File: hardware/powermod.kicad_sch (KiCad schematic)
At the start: 72 parts, among them J1 USB_C_IN, J2 USB_C_OUT, J3 JST_PH_2, J4 STEMMA_QT, J5 UPDI_HDR, Q1 AON7407, Q2 AON7407, Q3 BSS138, SW1 BUTTON, U1 BM8563, U2 ATtiny1617, U3 TPS63020DSJR, U4 TP4056, U5 XC6206P332MR, Y1 32.768kHz

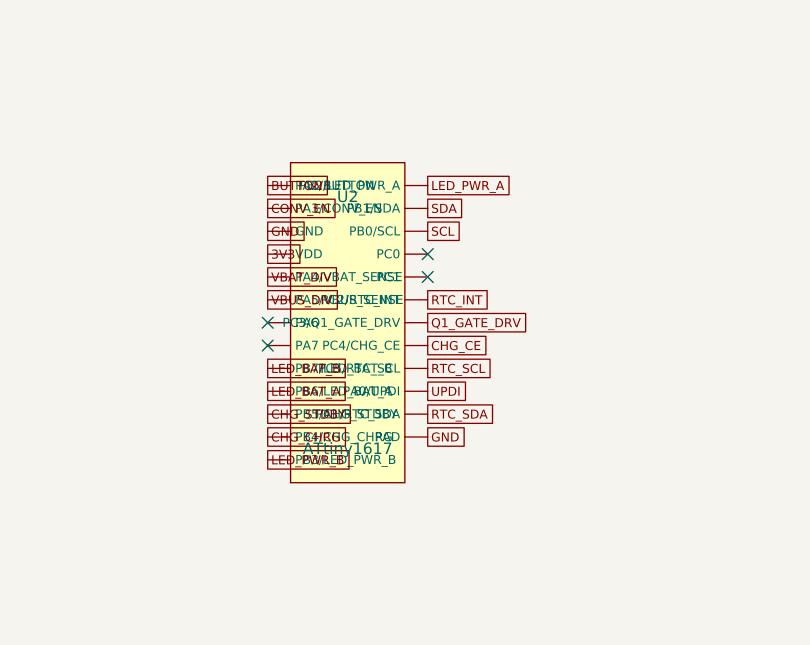
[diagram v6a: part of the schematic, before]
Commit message: attiny: swap MCU to ATtiny1616 SOIC-20 — breaks the QFN routing wall
The 24-pin QFN (0.5mm pitch) was the persistent autorouting blocker: two of
its pins could never escape, boxed in by their routed neighbours, and no
placement or router technique moved them. Swapping to the ATtiny1616 in
SOIC-20 (1.27mm pitch, 2.5x coarser, no exposed pad, hand-solderable) removes
that wall entirely -- verified: the MCU pins (3V3, Q1_GATE_DRV) that were stuck
across every prior attempt now route, and the residual is ordinary nets
(VBUS/VOUT pour connections, GND stitching), no escape wall.

Electrical: we used exactly 18 signals and the SOIC-20 has exactly 18 I/O, so
it fits -- at the cost of the 4 spare pins the 24-pin had. Four signals moved
off pins the 20-pin package lacks (LED_BAT_A/B off PB6/PB7 -> PA6/PA7, CHG_CE
off PC4 -> PC0, RTC_SCL off PC5 -> PC1); all are plain GPIO and the async-wake
(PC2/PA2), TWI (PB0/PB1), ADC (PA4/PA5) and UPDI (PA0) pins are unchanged.

Pinout taken from KiCad's ATtiny406-S base symbol (the shared 20-pin tinyAVR-1
map), NOT a web summary (which had it wrong). Footprint SOIC-20W_7.5x12.8mm.
LCSC C2891852 to confirm at order time. netlist self-test + ERC both clean
(72 components, 231 pins). On the attiny-soic20 branch.

Co-Authored-By: Claude Opus 4.8 <noreply@anthropic.com>
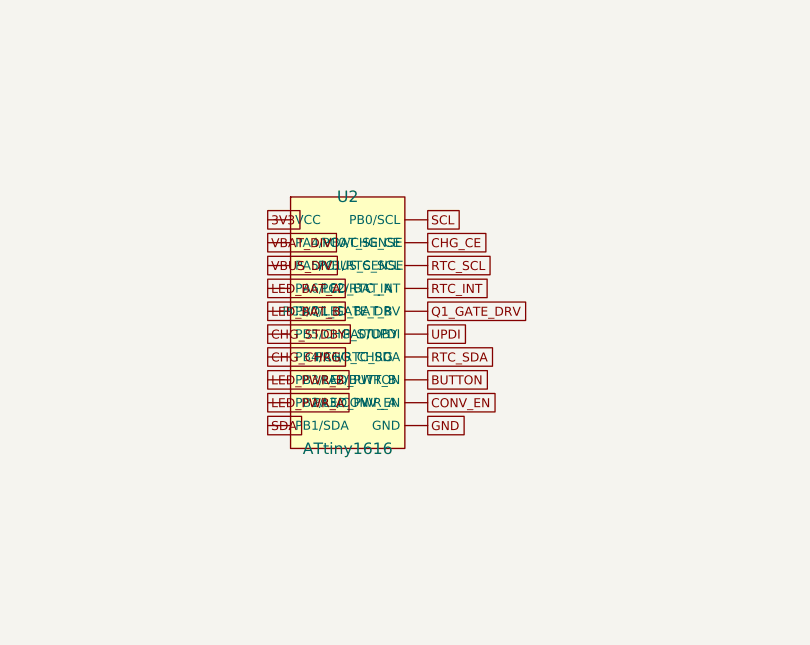
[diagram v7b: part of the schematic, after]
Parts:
- U2: value ATtiny1617 -> ATtiny1616; footprint Package_DFN_QFN:QFN-24-1EP_4x4mm_P0.5mm_EP2.6x2.6mm -> Package_SO:SOIC-20W_7.5x12.8mm_P1.27mm
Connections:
- net 3V3: now also U2.1 (VCC); no longer U2.4 (VDD)
- net BUTTON: now also U2.18 (PA2/BUTTON); no longer U2.1 (PA2/BUTTON)
- net CHG_CE: now also U2.12 (PC0/CHG_CE); no longer U2.21 (PC4/CHG_CE)
- net CHG_CHRG: now also U2.7 (PB4/CHG_CHRG); no longer U2.12 (PB4/CHG_CHRG)
- net CHG_STDBY: now also U2.6 (PB5/CHG_STDBY); no longer U2.11 (PB5/CHG_STDBY)
- net CONV_EN: now also U2.19 (PA3/CONV_EN); no longer U2.2 (PA3/CONV_EN)
- net GND: now also U2.20 (GND); no longer U2.25 (PAD), U2.3 (GND)
- net LED_BAT_A: now also U2.4 (PA6/LED_BAT_A); no longer U2.10 (PB6/LED_BAT_A)
- net LED_BAT_B: now also U2.5 (PA7/LED_BAT_B); no longer U2.9 (PB7/LED_BAT_B)
- net LED_PWR_A: now also U2.9 (PB2/LED_PWR_A); no longer U2.14 (PB2/LED_PWR_A)
- net LED_PWR_B: now also U2.8 (PB3/LED_PWR_B); no longer U2.13 (PB3/LED_PWR_B)
- net Q1_GATE_DRV: now also U2.15 (PC3/Q1_GATE_DRV); no longer U2.20 (PC3/Q1_GATE_DRV)
- net RTC_INT: now also U2.14 (PC2/RTC_INT); no longer U2.19 (PC2/RTC_INT)
- net RTC_SCL: now also U2.13 (PC1/RTC_SCL); no longer U2.22 (PC5/RTC_SCL)
- net RTC_SDA: now also U2.17 (PA1/RTC_SDA); no longer U2.24 (PA1/RTC_SDA)
- net SCL: now also U2.11 (PB0/SCL); no longer U2.16 (PB0/SCL)
- net SDA: now also U2.10 (PB1/SDA); no longer U2.15 (PB1/SDA)
- net UPDI: now also U2.16 (PA0/UPDI); no longer U2.23 (PA0/UPDI)
- net VBAT_DIV: now also U2.2 (PA4/VBAT_SENSE); no longer U2.5 (PA4/VBAT_SENSE)
- net VBUS_DIV: now also U2.3 (PA5/VBUS_SENSE); no longer U2.6 (PA5/VBUS_SENSE)
- no-connect marks 15 -> 11
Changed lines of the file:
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@@
  (symbol (lib_id "powermod:PM_U2") (at 670.5600000000001 294.64000000000004 0) (unit 1) (in_bom yes) (on_board yes)
   (property "Reference" "U2" (at 670.5600000000001 280.64000000000004 0) (effects (font (size 1.27 1.27))))
-  (property "Value" "ATtiny1617" (at 670.5600000000001 308.64000000000004 0) (effects (font (size 1.27 1.27))))
-  (property "Footprint" "Package_DFN_QFN:QFN-24-1EP_4x4mm_P0.5mm_EP2.6x2.6mm" (at 670.5600000000001 294.64000000000004 0) (effects (font (size 1.27 1.27)) hide))
+  (property "Value" "ATtiny1616" (at 670.5600000000001 308.64000000000004 0) (effects (font (size 1.27 1.27))))
+  (property "Footprint" "Package_SO:SOIC-20W_7.5x12.8mm_P1.27mm" (at 670.5600000000001 294.64000000000004 0) (effects (font (size 1.27 1.27)) hide))
   (pin "1")
   (pin "2")
@@
   (pin "18")
   (pin "19")
-  (pin "20")
-  (pin "21")
-  (pin "22")
-  (pin "23")
-  (pin "24")
-  (pin "25"))
+  (pin "20"))
  (symbol (lib_id "powermod:PM_U3") (at 670.5600000000001 360.68000000000006 0) (unit 1) (in_bom yes) (on_board yes)
   (property "Reference" "U3" (at 670.5600000000001 346.68000000000006 0) (effects (font (size 1.27 1.27))))
@@
  (global_label "RTC_SCL" (shape passive) (at 679.45 227.32999999999998 0) (effects (font (size 1.0 1.0)) (justify left)))
  (global_label "RTC_VDD" (shape passive) (at 679.45 232.41 0) (effects (font (size 1.0 1.0)) (justify left)))
- (global_label "BUTTON" (shape passive) (at 661.6700000000001 279.40000000000003 0) (effects (font (size 1.0 1.0)) (justify left)))
- (global_label "CONV_EN" (shape passive) (at 661.6700000000001 281.94000000000005 0) (effects (font (size 1.0 1.0)) (justify left)))
- (global_label "GND" (shape passive) (at 661.6700000000001 284.48 0) (effects (font (size 1.0 1.0)) (justify left)))
- (global_label "3V3" (shape passive) (at 661.6700000000001 287.02000000000004 0) (effects (font (size 1.0 1.0)) (justify left)))
- (global_label "VBAT_DIV" (shape passive) (at 661.6700000000001 289.56000000000006 0) (effects (font (size 1.0 1.0)) (justify left)))
- (global_label "VBUS_DIV" (shape passive) (at 661.6700000000001 292.1 0) (effects (font (size 1.0 1.0)) (justify left)))
- (global_label "LED_BAT_B" (shape passive) (at 661.6700000000001 299.72 0) (effects (font (size 1.0 1.0)) (justify left)))
- (global_label "LED_BAT_A" (shape passive) (at 661.6700000000001 302.26000000000005 0) (effects (font (size 1.0 1.0)) (justify left)))
- (global_label "CHG_STDBY" (shape passive) (at 661.6700000000001 304.80000000000007 0) (effects (font (size 1.0 1.0)) (justify left)))
- (global_label "CHG_CHRG" (shape passive) (at 661.6700000000001 307.34000000000003 0) (effects (font (size 1.0 1.0)) (justify left)))
- (global_label "LED_PWR_B" (shape passive) (at 661.6700000000001 309.88000000000005 0) (effects (font (size 1.0 1.0)) (justify left)))
- (global_label "LED_PWR_A" (shape passive) (at 679.45 279.40000000000003 0) (effects (font (size 1.0 1.0)) (justify left)))
- (global_label "SDA" (shape passive) (at 679.45 281.94000000000005 0) (effects (font (size 1.0 1.0)) (justify left)))
- (global_label "SCL" (shape passive) (at 679.45 284.48 0) (effects (font (size 1.0 1.0)) (justify left)))
- (global_label "RTC_INT" (shape passive) (at 679.45 292.1 0) (effects (font (size 1.0 1.0)) (justify left)))
- (global_label "Q1_GATE_DRV" (shape passive) (at 679.45 294.64000000000004 0) (effects (font (size 1.0 1.0)) (justify left)))
- (global_label "CHG_CE" (shape passive) (at 679.45 297.18000000000006 0) (effects (font (size 1.0 1.0)) (justify left)))
- (global_label "RTC_SCL" (shape passive) (at 679.45 299.72 0) (effects (font (size 1.0 1.0)) (justify left)))
- (global_label "UPDI" (shape passive) (at 679.45 302.26000000000005 0) (effects (font (size 1.0 1.0)) (justify left)))
- (global_label "RTC_SDA" (shape passive) (at 679.45 304.80000000000007 0) (effects (font (size 1.0 1.0)) (justify left)))
- (global_label "GND" (shape passive) (at 679.45 307.34000000000003 0) (effects (font (size 1.0 1.0)) (justify left)))
+ (global_label "3V3" (shape passive) (at 661.6700000000001 283.21000000000004 0) (effects (font (size 1.0 1.0)) (justify left)))
+ (global_label "VBAT_DIV" (shape passive) (at 661.6700000000001 285.75000000000006 0) (effects (font (size 1.0 1.0)) (justify left)))
+ (global_label "VBUS_DIV" (shape passive) (at 661.6700000000001 288.29 0) (effects (font (size 1.0 1.0)) (justify left)))
+ (global_label "LED_BAT_A" (shape passive) (at 661.6700000000001 290.83000000000004 0) (effects (font (size 1.0 1.0)) (justify left)))
+ (global_label "LED_BAT_B" (shape passive) (at 661.6700000000001 293.37000000000006 0) (effects (font (size 1.0 1.0)) (justify left)))
+ (global_label "CHG_STDBY" (shape passive) (at 661.6700000000001 295.91 0) (effects (font (size 1.0 1.0)) (justify left)))
+ (global_label "CHG_CHRG" (shape passive) (at 661.6700000000001 298.45000000000005 0) (effects (font (size 1.0 1.0)) (justify left)))
+ (global_label "LED_PWR_B" (shape passive) (at 661.6700000000001 300.99000000000007 0) (effects (font (size 1.0 1.0)) (justify left)))
+ (global_label "LED_PWR_A" (shape passive) (at 661.6700000000001 303.53000000000003 0) (effects (font (size 1.0 1.0)) (justify left)))
+ (global_label "SDA" (shape passive) (at 661.6700000000001 306.07000000000005 0) (effects (font (size 1.0 1.0)) (justify left)))
+ (global_label "SCL" (shape passive) (at 679.45 283.21000000000004 0) (effects (font (size 1.0 1.0)) (justify left)))
+ (global_label "CHG_CE" (shape passive) (at 679.45 285.75000000000006 0) (effects (font (size 1.0 1.0)) (justify left)))
+ (global_label "RTC_SCL" (shape passive) (at 679.45 288.29 0) (effects (font (size 1.0 1.0)) (justify left)))
+ (global_label "RTC_INT" (shape passive) (at 679.45 290.83000000000004 0) (effects (font (size 1.0 1.0)) (justify left)))
+ (global_label "Q1_GATE_DRV" (shape passive) (at 679.45 293.37000000000006 0) (effects (font (size 1.0 1.0)) (justify left)))
+ (global_label "UPDI" (shape passive) (at 679.45 295.91 0) (effects (font (size 1.0 1.0)) (justify left)))
+ (global_label "RTC_SDA" (shape passive) (at 679.45 298.45000000000005 0) (effects (font (size 1.0 1.0)) (justify left)))
+ (global_label "BUTTON" (shape passive) (at 679.45 300.99000000000007 0) (effects (font (size 1.0 1.0)) (justify left)))
+ (global_label "CONV_EN" (shape passive) (at 679.45 303.53000000000003 0) (effects (font (size 1.0 1.0)) (justify left)))
+ (global_label "GND" (shape passive) (at 679.45 306.07000000000005 0) (effects (font (size 1.0 1.0)) (justify left)))
  (global_label "VSYS" (shape passive) (at 661.6700000000001 351.7900000000001 0) (effects (font (size 1.0 1.0)) (justify left)))
  (global_label "GND" (shape passive) (at 661.6700000000001 354.33000000000004 0) (effects (font (size 1.0 1.0)) (justify left)))
@@
  (no_connect (at 234.95 163.83))
  (no_connect (at 679.45 229.87))
- (no_connect (at 661.6700000000001 294.64000000000004))
- (no_connect (at 661.6700000000001 297.18000000000006))
- (no_connect (at 679.45 287.02000000000004))
- (no_connect (at 679.45 289.56000000000006))
  (no_connect (at 679.45 364.49000000000007))
 )

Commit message: hardware: pre-fab audit + D5 supercap-drain fix; mount board final
Full pre-fab audit (PREFAB_AUDIT.md): board verified pad-for-pad against
netlist.py (214/214 + 11 NC), every IC pinout re-checked against datasheets,
all operating points computed (FB divider exactly 5.000/3.278V via JP2, ADC
ranges, gate drive, ~7.5uA off-state drain). Findings fixed:

- D5 (1N4148WS) added in the VBACKUP charge path (3V3 -> R27 -> D5 -> JP1,
  new net CHG_JPD): without it the supercap back-drains through R27 into the
  dead 3V3 rail at ~3mA exactly when backup is needed.
- 2 PGND vias added in U3's exposed pad (the TPS63020 4A power-ground return
  had no via to the In1 plane within 3.5mm).
- USB-C merged-pad footprint lib (powermod.pretty) now tracked; J1/J2 use it.
- finish_board.py: reusable SES-import + GND-stitch + island-tie + refill
  finisher. place_constrained.py: constraint-aware force-directed placer.

Board state: 0 unconnected, 0 clearance; only the 4 intrinsic track_width
necks at U3's 0.65mm pins remain. Placement + USB-C escapes are hand-routed
(never regenerate the board from netlist.py).

Co-Authored-By: Claude Opus 4.8 <noreply@anthropic.com>
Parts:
- added D5: 1N4148WS, Diode_SMD:D_SOD-323, symbol powermod:PM_D5
- J1, J2: footprint Connector_USB:USB_C_Receptacle_HRO_TYPE-C-31-M-12 -> powermod:USB_C_Receptacle_TYPE-C_16P_PowerMerged
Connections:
- net CHG_JP: now also D5.2 (A); no longer JP1.1 (A)
- net GND: now also J1.SH (SHIELD), J2.SH (SHIELD); no longer J1.B1 (GND), J1.B12 (GND), J1.S1 (SHIELD), J2.B1 (GND), J2.B12 (GND), J2.S1 (SHIELD)
- net VBUS: no longer J1.B4 (VBUS), J1.B9 (VBUS)
- net VOUT: no longer J2.B4 (VBUS), J2.B9 (VBUS)
- new net CHG_JPD: D5.1 (K), JP1.1 (A)
